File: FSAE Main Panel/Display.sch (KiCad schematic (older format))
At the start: 89 parts, among them Q501 SI2308CDS-T1-GE3, Q502 SI2308CDS-T1-GE3, U501 TLC6C598, U502 TLC6C5816, U503 TLC6C5816, U504 TLC6C5816

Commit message: Power Supply Changes Again
Shrunk some 5V layout by switching LM7805's for their SOT223 packages but with very careful top copper considerations for thermal management.
Shrunk the Right side by 12mm for more clearance near ignition button.
Fixed Shift Register clock signal routing.
Changed shift order to be 7 segment first for easiler routing.
Added Mounting Holes.
TODO: Figure out Top layer 7 segment placement.
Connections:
- net RPM_SCLK is gone; now on net SCLK: U502.17 (SRCK), U503.17 (SRCK), U504.17 (SRCK)
- net a: now also RN501.1 (R1.1); no longer RN501.16 (R1.2)
- net aI: now also RN501.16 (R1.2); no longer RN501.1 (R1.1)
- net b: now also RN501.2 (R2.1); no longer RN501.15 (R2.2)
- net bI: now also RN501.15 (R2.2); no longer RN501.2 (R2.1)
- net c: now also RN501.3 (R3.1); no longer RN501.14 (R3.2)
- net cI: now also RN501.14 (R3.2); no longer RN501.3 (R3.1)
- net d: now also RN501.4 (R4.1); no longer RN501.13 (R4.2)
- net dI: now also RN501.13 (R4.2); no longer RN501.4 (R4.1)
- net e: now also RN501.5 (R5.1); no longer RN501.12 (R5.2)
- net eI: now also RN501.12 (R5.2); no longer RN501.5 (R5.1)
- net f: now also RN501.6 (R6.1); no longer RN501.11 (R6.2)
- net fI: now also RN501.11 (R6.2); no longer RN501.6 (R6.1)
- net g: now also RN501.7 (R7.1); no longer RN501.10 (R7.2)
- net gI: now also RN501.10 (R7.2); no longer RN501.7 (R7.1)
- net GEAR_OUT: now reaches U501.9 (SER_OUT)
- net at U502.15 (SER_OUT): now also U504.12 (SER_IN); no longer U503.12 (SER_IN)
- net at U503.15 (SER_OUT): no longer U504.12 (SER_IN)
- net GEAR_SCLK renamed SCLK
- net RPM_OUT: no longer names the net of U504.15 (SER_OUT)
- net RPM_OUT: now also U503.12 (SER_IN)
- no-connect marks 18 -> 19
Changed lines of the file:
@@
 F 4 "4816P-1-510LF" V 4400 6700 60  0001 C CNN "Part Number"
 	1    4400 6700
-	0    1    1    0
+	0    -1   1    0
 $EndComp
 $Comp
@@
 Text GLabel 1250 7200 0    60   Input ~ 0
 GEAR_RCLK
-NoConn ~ 3550 7050
 $Comp
 L Device:C C502
@@
 $EndComp
 Text GLabel 1250 6600 0    60   Input ~ 0
-GEAR_SCLK
+SCLK
 Text GLabel 1250 6750 0    60   Input ~ 0
 GEAR_IN
@@
 RPM_IN
 Text GLabel 1000 5500 0    39   Input ~ 0
-RPM_SCLK
+SCLK
 Text GLabel 1000 5400 0    39   Input ~ 0
 RPM_RCLK
-Text GLabel 1000 5600 0    39   Input ~ 0
-RPM_OUT
 $Comp
 L power:+3.3V #PWR0504
@@
 	1200 3450 1200 3350
 Wire Wire Line
-	2550 4800 3000 4800
-Wire Wire Line
 	3000 4600 3150 4600
 Wire Wire Line
-	4250 4800 4700 4800
-Wire Wire Line
-	4700 4800 4700 4600
-Wire Wire Line
 	4700 4600 4850 4600
 Wire Wire Line
@@
 	3150 4500 2950 4500
 Wire Wire Line
-	3000 4800 3000 4600
-Wire Wire Line
 	2650 4700 2650 5400
 Wire Wire Line
@@
 	2700 4600 2700 5500
 Connection ~ 2700 5500
-Wire Wire Line
-	1000 5600 5950 5600
-Wire Wire Line
-	5950 5600 5950 4800
 Text Label 2500 7050 0    39   ~ 0
 ~G7
@@
 Wire Wire Line
 	5450 900  6000 900
+Wire Wire Line
+	5950 5000 5950 4800
+Wire Wire Line
+	3000 4600 3000 5000
+NoConn ~ 4250 4800
+Wire Wire Line
+	4700 4600 4700 5050
+Wire Wire Line
+	4700 5050 2550 5050
+Wire Wire Line
+	2550 5050 2550 4800
+Wire Wire Line
+	3550 7400 3550 7050
+Text GLabel 1250 7350 0    60   Input ~ 0
+GEAR_OUT
+Wire Wire Line
+	1250 7400 1250 7350
+Wire Wire Line
+	1250 7400 3550 7400
+NoConn ~ -14750 5700
 Wire Bus Line
 	1300 2900 1300 3600
@@
 Wire Bus Line
 	3000 2900 3000 3600
+Wire Wire Line
+	3000 5000 5950 5000
 Wire Bus Line
 	1300 5100 6600 5100

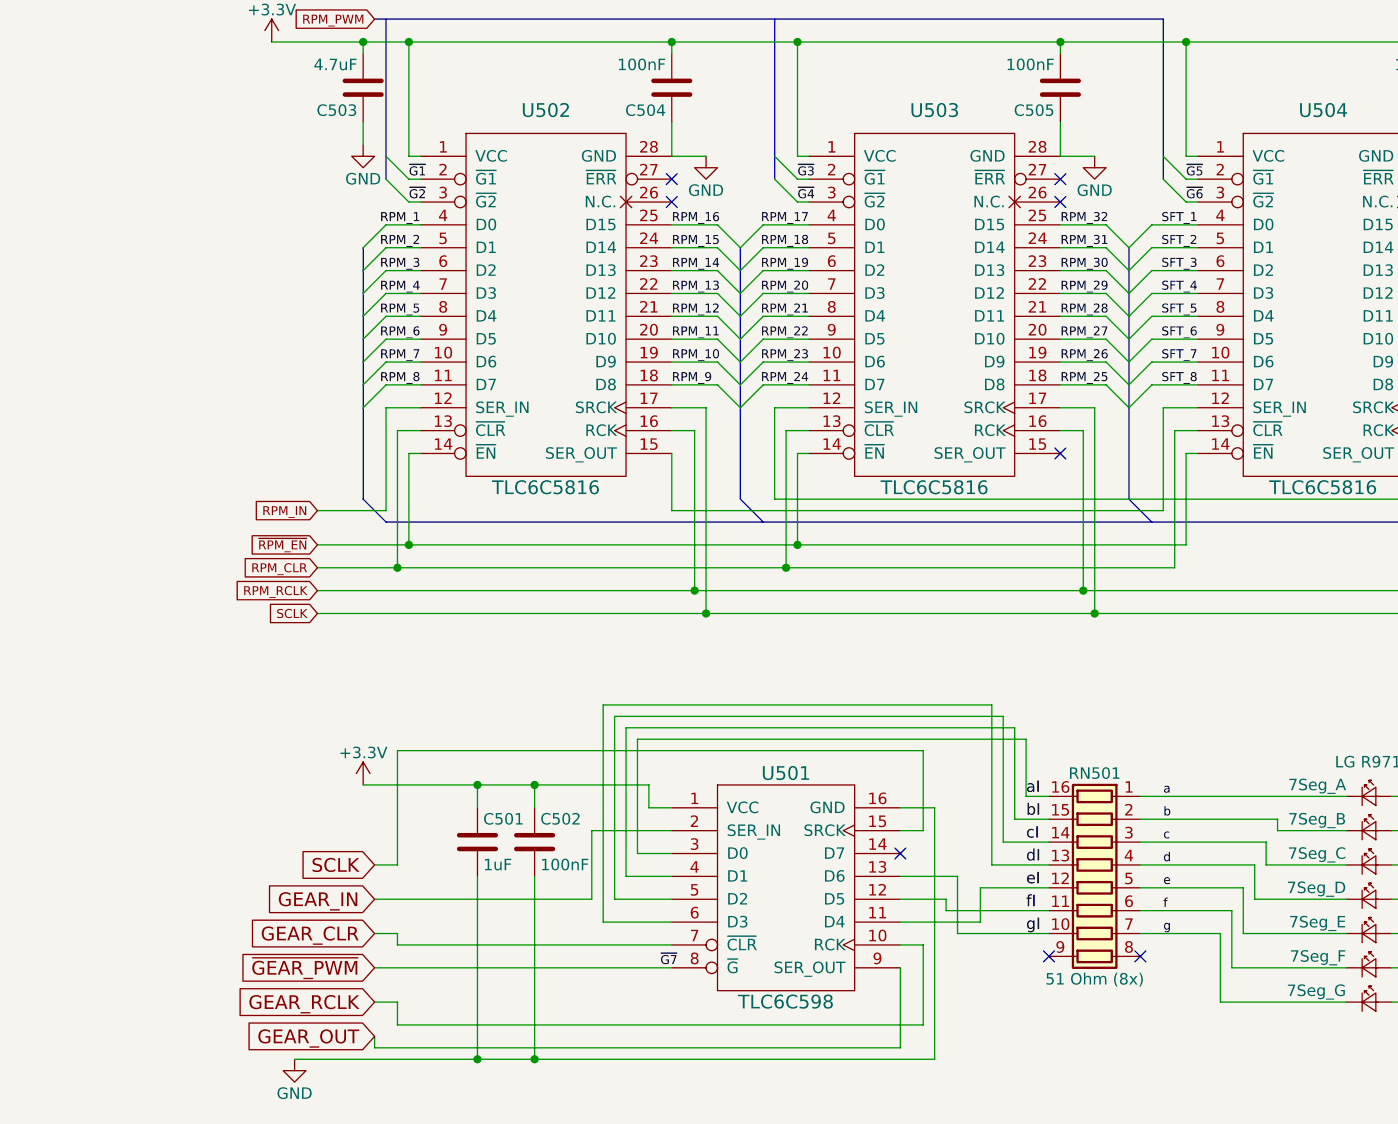
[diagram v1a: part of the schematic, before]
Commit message: Most Signal Routing
Todo: Figure out 7 segment LED placements and route their power traces
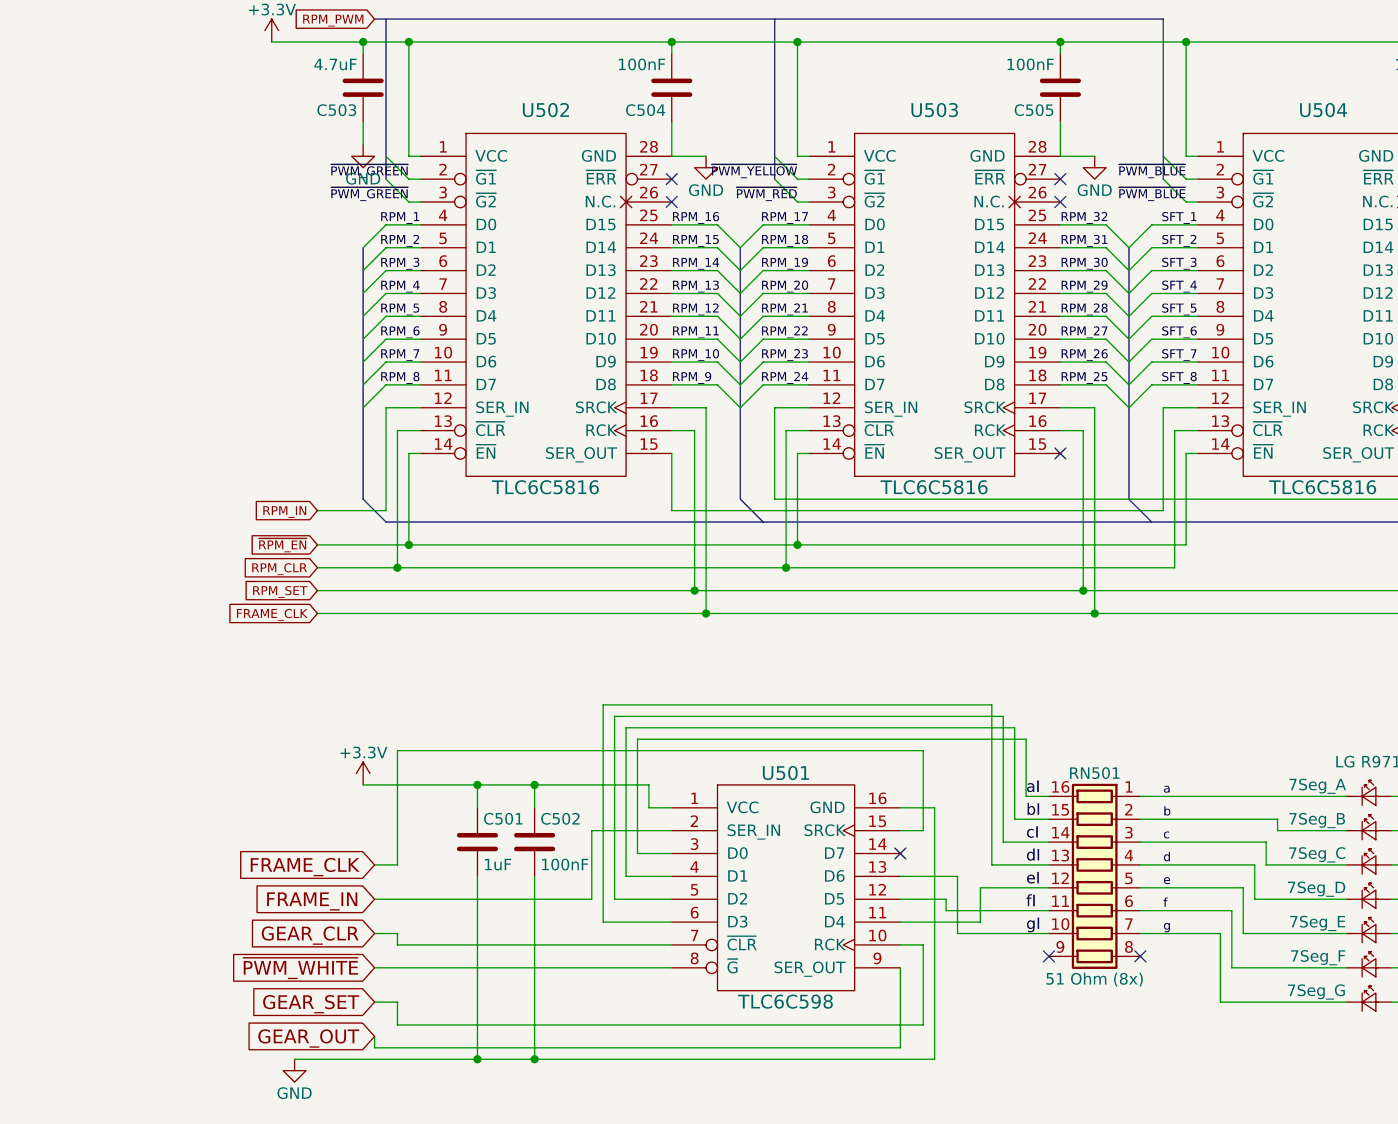
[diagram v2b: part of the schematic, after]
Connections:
- net ~G2 is gone; now on net ~PWM_GREEN: U502.3 (~G2)
- net ~G6 is gone; now on net ~PWM_BLUE: U504.3 (~G2)
- net GEAR_IN renamed FRAME_IN
- net GEAR_RCLK renamed GEAR_SET
- net RPM_RCLK renamed RPM_SET
- net SCLK renamed FRAME_CLK
- net ~G1 renamed ~PWM_GREEN
- net ~G3 renamed ~PWM_YELLOW
- net ~G4 renamed ~PWM_RED
- net ~G5 renamed ~PWM_BLUE
- net ~GEAR_PWM renamed ~PWM_WHITE
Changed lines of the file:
@@
 $EndComp
 Text GLabel 1250 7050 0    60   Input ~ 0
-~GEAR_PWM
+~PWM_WHITE
 Text GLabel 1250 6900 0    60   Input ~ 0
 GEAR_CLR
 Text GLabel 1250 7200 0    60   Input ~ 0
-GEAR_RCLK
+GEAR_SET
 $Comp
 L Device:C C502
@@
 $EndComp
 Text GLabel 1250 6600 0    60   Input ~ 0
-SCLK
+FRAME_CLK
 Text GLabel 1250 6750 0    60   Input ~ 0
-GEAR_IN
+FRAME_IN
 $Comp
 L Device:C C501
@@
 F 1 "TLC6C5816" H 2000 3450 60  0000 C CNN
 F 2 "TLC6C5816:TLC6C5816" H 2050 3500 60  0001 C CNN
-F 3 "" H 2050 3500 60  0001 C CNN
+F 3 "http://www.ti.com/lit/ds/symlink/tlc6c5816-q1.pdf" H 2050 3500 60  0001 C CNN
 	1    2000 4200
 	1    0    0    -1
@@
 F 1 "TLC6C5816" H 3700 3450 60  0000 C CNN
 F 2 "TLC6C5816:TLC6C5816" H 3750 3500 60  0001 C CNN
-F 3 "" H 3750 3500 60  0001 C CNN
+F 3 "http://www.ti.com/lit/ds/symlink/tlc6c5816-q1.pdf" H 3750 3500 60  0001 C CNN
 	1    3700 4200
 	1    0    0    -1
@@
 F 1 "TLC6C5816" H 5400 3450 60  0000 C CNN
 F 2 "TLC6C5816:TLC6C5816" H 5450 3500 60  0001 C CNN
-F 3 "" H 5450 3500 60  0001 C CNN
+F 3 "http://www.ti.com/lit/ds/symlink/tlc6c5816-q1.pdf" H 5450 3500 60  0001 C CNN
 	1    5400 4200
 	1    0    0    -1
@@
 RPM_IN
 Text GLabel 1000 5500 0    39   Input ~ 0
-SCLK
+FRAME_CLK
 Text GLabel 1000 5400 0    39   Input ~ 0
-RPM_RCLK
+RPM_SET
 $Comp
 L power:+3.3V #PWR0504
@@
 Wire Wire Line
 	1450 3700 1400 3700
-Text Label 1400 3600 0    39   ~ 0
-~G1
-Text Label 1400 3700 0    39   ~ 0
-~G2
-Text Label 3100 3600 0    39   ~ 0
-~G3
-Text Label 3100 3700 0    39   ~ 0
-~G4
-Text Label 4800 3600 0    39   ~ 0
-~G5
-Text Label 4800 3700 0    39   ~ 0
-~G6
+Text Label 1400 3600 2    39   ~ 0
+~PWM_GREEN
+Text Label 3100 3600 2    39   ~ 0
+~PWM_YELLOW
+Text Label 3100 3700 2    39   ~ 0
+~PWM_RED
+Text Label 4800 3600 2    39   ~ 0
+~PWM_BLUE
+Text Label 4800 3700 2    39   ~ 0
+~PWM_BLUE
 Wire Bus Line
 	11100 3000 11100 2750
@@
 	2700 4600 2700 5500
 Connection ~ 2700 5500
-Text Label 2500 7050 0    39   ~ 0
-~G7
 Wire Wire Line
 	1700 6250 1950 6250
@@
 Wire Bus Line
 	6450 2750 11100 2750
+Text Label 1400 3700 2    39   ~ 0
+~PWM_GREEN
 $EndSCHEMATC

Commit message: Version 1
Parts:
- added HS1, HS2, HS3: Heatsink_Pad, Measurement_Points:Measurement_Point_Round-TH_Small, symbol Mechanical:Heatsink_Pad
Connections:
- net LED_5V+ is gone; now on net LED_+5V: D562.2 (A), D563.2 (A), D564.2 (A), D565.2 (A), D566.2 (A), D567.2 (A), D568.2 (A)
- new net HEAT1: HS1.1
- new net HEAT2: HS2.1
- new net HEAT3: HS3.1
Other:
- note removed: "OSRAM LB M673\nVf = 3.7V, If = 20mA\n45mcd"
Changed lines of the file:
@@
 $EndComp
 Text GLabel 5850 6100 2    60   Input ~ 0
-LED_5V+
+LED_+5V
 $Comp
 L power:GND #PWR0502
@@
 	-1   0    0    1
 $EndComp
-Text Notes 7700 4400 0    35   ~ 0
-OSRAM LB M673\nVf = 3.7V, If = 20mA\n45mcd
 $Comp
 L Device:R_Pack08 RN507
@@
 Entry Wire Line
 	1300 3600 1400 3700
-Wire Bus Line
-	4700 2900 1250 2900
-Text GLabel 1250 2900 0    39   Input ~ 0
-RPM_PWM
 Wire Wire Line
 	4850 3600 4800 3600
@@
 	1250 7400 3550 7400
 NoConn ~ -14750 5700
+Text Label 1400 3700 2    39   ~ 0
+~PWM_GREEN
+Connection ~ 3000 2900
+Wire Bus Line
+	3000 2900 1300 2900
+Entry Wire Line
+	5000 2550 5100 2450
+Entry Wire Line
+	5000 2400 5100 2300
+Entry Wire Line
+	5000 2250 5100 2150
+Entry Wire Line
+	5000 2100 5100 2000
+Text GLabel 5150 2000 2    39   Input ~ 0
+~PWM_GREEN
+Text Label 5100 2000 2    39   ~ 0
+~PWM_GREEN
+Text GLabel 5150 2150 2    39   Input ~ 0
+~PWM_YELLOW
+Text GLabel 5150 2300 2    39   Input ~ 0
+~PWM_RED
+Text GLabel 5150 2450 2    39   Input ~ 0
+~PWM_BLUE
+Text Label 5100 2150 2    39   ~ 0
+~PWM_YELLOW
+Text Label 5100 2300 2    39   ~ 0
+~PWM_RED
+Text Label 5100 2450 2    39   ~ 0
+~PWM_BLUE
+Wire Wire Line
+	5100 2450 5150 2450
+Wire Wire Line
+	5100 2300 5150 2300
+Wire Wire Line
+	5100 2150 5150 2150
+Wire Wire Line
+	5100 2000 5150 2000
+Wire Bus Line
+	3000 2900 4700 2900
+Wire Bus Line
+	5000 2900 4700 2900
+Connection ~ 4700 2900
+$Comp
+L Mechanical:Heatsink_Pad HS1
+U 1 1 5CCF152A
+P 6900 3850
+F 0 "HS1" V 7100 3900 50  0000 L CNN
+F 1 "Heatsink_Pad" V 7100 3300 50  0000 L CNN
+F 2 "Measurement_Points:Measurement_Point_Round-TH_Small" H 6912 3800 50  0001 C CNN
+F 3 "~" H 6912 3800 50  0001 C CNN
+	1    6900 3850
+	0    -1   -1   0
+$EndComp
+Text GLabel 7000 3850 2    50   Input ~ 0
+HEAT1
+$Comp
+L Mechanical:Heatsink_Pad HS2
+U 1 1 5CFF1846
+P 6900 4350
+F 0 "HS2" V 7100 4400 50  0000 L CNN
+F 1 "Heatsink_Pad" V 7050 3800 50  0000 L CNN
+F 2 "Measurement_Points:Measurement_Point_Round-TH_Small" H 6912 4300 50  0001 C CNN
+F 3 "~" H 6912 4300 50  0001 C CNN
+	1    6900 4350
+	0    -1   -1   0
+$EndComp
+Text GLabel 7000 4350 2    50   Input ~ 0
+HEAT2
+$Comp
+L Mechanical:Heatsink_Pad HS3
+U 1 1 5D0512E1
+P 6900 4800
+F 0 "HS3" V 7100 4850 50  0000 L CNN
+F 1 "Heatsink_Pad" V 7050 4250 50  0000 L CNN
+F 2 "Measurement_Points:Measurement_Point_Round-TH_Small" H 6912 4750 50  0001 C CNN
+F 3 "~" H 6912 4750 50  0001 C CNN
+	1    6900 4800
+	0    -1   -1   0
+$EndComp
+Text GLabel 7000 4800 2    50   Input ~ 0
+HEAT3
 Wire Bus Line
 	1300 2900 1300 3600
+Wire Wire Line
+	3000 5000 5950 5000
+Wire Bus Line
+	3000 2900 3000 3600
 Wire Bus Line
 	4700 2900 4700 3600
 Wire Bus Line
-	3000 2900 3000 3600
-Wire Wire Line
-	3000 5000 5950 5000
-Wire Bus Line
 	1300 5100 6600 5100
 Wire Bus Line
-	1200 3900 1200 5000
+	5000 2100 5000 2900
+Wire Bus Line
+	4550 3900 4550 5000
+Wire Bus Line
+	2850 3900 2850 5000
 Wire Bus Line
 	6250 3900 6250 5000
 Wire Bus Line
-	2850 3900 2850 5000
-Wire Bus Line
-	4550 3900 4550 5000
+	1200 3900 1200 5000
 Wire Bus Line
 	6600 3000 11100 3000
 Wire Bus Line
 	6450 2750 11100 2750
-Text Label 1400 3700 2    39   ~ 0
-~PWM_GREEN
 $EndSCHEMATC

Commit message: Manufacturing Tweaks
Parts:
- D502, D503, D504, D505, D506, D507, D508, D509, D510, D511, D512, D513, D514, D515, D516, D517, D562, D563, D564, D565, D566, D567, D568: Manufacturer OSRAM -> Kingbright; Part Number (none) -> APD3224ZGCK-F01
- D518, D519, D520, D521, D522, D523, D524, D525, D526, D527, D528, D529, D530, D531, D532, D533, D534, D535, D536, D537, D538, D539, D540, D541, D542, D543, D544, D545, D546, D547, D548, D549, D550, D551, D552, D553, D554, D555, D556, D557, D558, D559, D560, D561: Manufacturer OSRAM -> Kingbright
